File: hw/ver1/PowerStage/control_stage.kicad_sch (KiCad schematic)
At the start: 3 parts, among them J10 SWD Debug, P1 USB_C_Plug_USB2.0, U10 RP2040

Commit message: Sync morning work to laptop
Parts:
- added C18, C21: 4.7uF, Capacitor_SMD:C_0603_1608Metric, symbol Device:C
- added J11: BMS_Serial, Connector_PinHeader_2.54mm:PinHeader_1x03_P2.54mm_Vertical, symbol Connector:Conn_01x03_Pin
- added J8: FanConnector, Connector_Molex:Molex_KK-254_AE-6410-04A_1x04_P2.54mm_Vertical, symbol Connector:Conn_01x04_Pin
- added JP3: I2C_Master, symbol Jumper:SolderJumper_2_Open
- added R92: 10k, Resistor_SMD:R_0603_1608Metric, symbol Device:R_US
- added SW2: I2C_Addr, Button_Switch_SMD:SW_DIP_SPSTx03_Slide_6.7x9.18mm_W6.73mm_P2.54mm_LowProfile_JPin, symbol Switch:SW_DIP_x03
- added U4: LM1117MP-3.3, Package_TO_SOT_SMD:SOT-223-3_TabPin2, symbol Regulator_Linear:LM1117MP-3.3
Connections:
- new net +12P: J8.2 (Pin_2)
- new net +3.3VP: C21.1, R92.2, U4.2 (VO)
- new net +5P: C18.1, U4.3 (VI)
- new net FAN_CTRL: J8.4 (Pin_4)
- new net FAN_SENSE: J8.3 (Pin_3), R92.1
- new net GND: C18.2, C21.2, J8.1 (Pin_1), U4.1 (GND)

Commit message: Sync this morning's effort
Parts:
- added C71, C79: 15pF, Capacitor_SMD:C_0603_1608Metric, symbol Device:C
- added C80, C81, C89: 4.7uF, Capacitor_SMD:C_0603_1608Metric, symbol Device:C
- added C82, C83, C84, C85, C86, C87, C88, C90, C91, C92, C93: 100nF, Capacitor_SMD:C_0603_1608Metric, symbol Device:C
- added D4: B5819W, Diode_SMD:D_SOD-123, symbol Device:D_Schottky
- added R107: 1k, Resistor_SMD:R_0603_1608Metric, symbol Device:R_US
- added R108, R109: 5.1k, Resistor_SMD:R_0603_1608Metric, symbol Device:R_US
- added R24, R26: 22, Resistor_SMD:R_0603_1608Metric, symbol Device:R_US
- added R28, R30: 10k, Resistor_SMD:R_0603_1608Metric, symbol Device:R_US
- added SW3: Boot, symbol Switch:SW_Push
- added SW4: Reset, symbol Switch:SW_Push
- added U20: W25Q32JVZP, Package_SON:WSON-8-1EP_6x5mm_P1.27mm_EP3.4x4.3mm, symbol Memory_Flash:W25Q32JVZP
- added U21: LM1117MP-5.0, Package_TO_SOT_SMD:SOT-223-3_TabPin2, symbol Regulator_Linear:LM1117MP-5.0
- added Y1: 12MHz, Crystal:Crystal_SMD_3225-4Pin_3.2x2.5mm_HandSoldering, symbol Device:Crystal_GND24
- P1: symbol Connector:USB_C_Plug_USB2.0 -> Connector:USB_C_Receptacle_USB2.0_16P
- U4: LCSC C23984 -> C6186
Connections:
- net +3.3VP is gone; now on net +3.3V: C21.1, R92.2, U4.2 (VO)
- net GND: now also J10.3 (Pin_3), P1.A1 (GND), P1.A12 (GND), P1.B1 (GND), P1.B12 (GND), P1.S1 (SHIELD), U10.19 (TESTEN), U10.57 (GND), C71.1, C79.1, C80.2, C81.2, C82.2, C83.2, C84.2, C85.2, C86.2, C87.2, C88.2, C89.2, C90.2, C91.2, C92.2, C93.2, R108.1, R109.1, SW3.1, SW4.1, U20.4 (GND), U20.9 (EP), U21.1 (GND), Y1.2, Y1.4
- net +3.3V: now reaches U10.1 (IOVDD), U10.10 (IOVDD), U10.22 (IOVDD), U10.33 (IOVDD), U10.42 (IOVDD), U10.49 (IOVDD)
- net +3.3V: now also U10.43 (ADC_AVDD), U10.44 (VREG_IN), U10.48 (USB_VDD), C81.1, C82.1, C83.1, C84.1, C85.1, C86.1, C87.1, C88.1, C92.1, R28.2, U20.8 (VCC)
- net at U10.20 (XIN): now also C79.2, Y1.1
- net at U10.21 (XOUT): now also R107.2
- net at U10.23 (DVDD), U10.50 (DVDD): now also U10.45 (VREG_VOUT), C89.1, C90.1, C91.1
- net at U10.24 (SWCLK): now also J10.1 (Pin_1)
- net at U10.25 (SWD): now also J10.2 (Pin_2)
- net RUN: now reaches U10.26 (RUN)
- net RUN: now also C93.1, R28.1, SW4.2
- net at U10.46 (USB_DM): now also R26.1
- net at U10.47 (USB_DP): now also R24.1
- net at U10.51 (QSPI_SD3): now also U20.7 (IO3)
- net at U10.52 (QSPI_SCLK): now also U20.6 (CLK)
- net at U10.53 (QSPI_SD0): now also U20.5 (DI(IO0))
- net at U10.54 (QSPI_SD2): now also U20.3 (IO2)
- net at U10.55 (QSPI_SD1): now also U20.2 (DO(IO1))
- net QSPI_SS: now reaches U10.56 (QSPI_SS)
- net QSPI_SS: now also R30.2, U20.1 (~{CS})
- net at P1.A4 (VBUS), P1.A9 (VBUS), P1.B4 (VBUS)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: now also D4.2 (A)
- net at P1.A5 (CC1): now also R108.2
- net USB_D+: now reaches P1.A6 (D+)
- net USB_D+: now also P1.B6 (D+), R24.2
- net USB_D-: now reaches P1.A7 (D-)
- net USB_D-: now also P1.B7 (D-), R26.2
- net at P1.B5 (CC2): now also R109.2
- net +12P renamed +12V
- net +12V: now also C80.1, U21.3 (VI)
- net +5P renamed +5V
- net +5V: now also D4.1 (K), U21.2 (VO)
- new net: R30.1, SW3.2
- new net: C71.2, R107.1, Y1.3
- no-connect marks 0 -> 2
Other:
- note added: "Add some nice leds"
- moved on the sheet: C18, C21, J10, J11, U10, U4

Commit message: Sync tonight's effort
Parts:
- removed JP3: I2C_Master, symbol Jumper:SolderJumper_2_Open
- added C94: 4.7uF, Capacitor_SMD:C_0603_1608Metric, symbol Device:C
- added D5, D6: Yellow LED, LED_SMD:LED_0805_2012Metric, symbol Device:LED
- added R110, R111, R112, R113, R114, R115: 0, Resistor_SMD:R_0603_1608Metric, symbol Device:R_US
- added R116, R126, R127, R130: 100k, Resistor_SMD:R_0603_1608Metric, symbol Device:R_US
- added R117, R118, R119, R121, R122, R123, R128: 1k, Resistor_SMD:R_0603_1608Metric, symbol Device:R_US
- added R120, R124, R125, R129: 2k, Resistor_SMD:R_0603_1608Metric, symbol Device:R_US
- added R131, R132: 510, Resistor_SMD:R_0603_1608Metric, symbol Device:R_US
- D4: Digikey (none) -> N/A
- J10, J11: Digikey (none) -> N/A; LCSC (none) -> N/A
- J8, P1, U20, Y1: LCSC (none) -> N/A
- SW3, SW4: footprint (none) -> Button_Switch_SMD:SW_SPST_EVQP2; Digikey (none) -> P11081SCT-ND; LCSC (none) -> N/A
- U10: Digikey (none) -> 2648-SC0914(13)CT-ND; LCSC (none) -> C2040
- U21: Digikey (none) -> N/A; LCSC (none) -> C6187
- U4: Digikey 488-LM1117MPX-33NOPBCT-ND -> N/A
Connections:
- net +3.3V: now also R126.2, R127.2, R130.2
- net +5V: now also R131.1, R132.1
- net FAN_CTRL: now also U10.8 (GPIO6), R121.2; no longer J8.4 (Pin_4)
- net FAN_SENSE: now also U10.4 (GPIO2)
- net GND: now also J11.3 (Pin_3), SW2.4, SW2.5, SW2.6, C94.2, R120.1, R124.1, R125.1, R129.1
- net at U10.11 (GPIO8): now also R115.2
- net at U10.12 (GPIO9): now also R114.2
- net SPI1_SCK: now reaches U10.13 (GPIO10)
- net SPI1_SCK: now also R113.2
- net SPI1_TX: now reaches U10.14 (GPIO11)
- net SPI1_TX: now also R110.2
- net SPI1_RX: now reaches U10.15 (GPIO12)
- net SPI1_RX: now also R112.2
- net SPI1_CSn: now reaches U10.16 (GPIO13)
- net SPI1_CSn: now also R111.2
- net CTL_OUT_SYNC: now reaches U10.17 (GPIO14)
- net CTL_OUT_RUN: now reaches U10.18 (GPIO15)
- net at U10.2 (GPIO0): now also R116.2
- net CTL_OUT_CCM: now reaches U10.27 (GPIO16)
- net CTL_OUT_DCM: now reaches U10.28 (GPIO17)
- net LED_STATUS_0: now reaches U10.29 (GPIO18)
- net LED_STATUS_0: now also D6.1 (K)
- net LED_STATUS_1: now reaches U10.30 (GPIO19)
- net LED_STATUS_1: now also D5.1 (K)
- net I2C_ADDR_0: now reaches U10.31 (GPIO20)
- net I2C_ADDR_0: now also SW2.1, R126.1
- net I2C_ADDR_1: now reaches U10.32 (GPIO21)
- net I2C_ADDR_1: now also SW2.2, R127.1
- net I2C_ADDR_2: now reaches U10.34 (GPIO22)
- net I2C_ADDR_2: now also SW2.3, R130.1
- net CTL_OUT_ADC_SEL_0: now reaches U10.35 (GPIO23)
- net CTL_OUT_ADC_SEL_1: now reaches U10.36 (GPIO24)
- net CTL_OUT_ADC_SEL_2: now reaches U10.37 (GPIO25)
- net CTL_IN_ADC: now reaches U10.38 (GPIO26_ADC0)
- net UART1_TX: now reaches U10.6 (GPIO4)
- net UART1_TX: now also R118.2
- net UART1_RX: now reaches U10.7 (GPIO5)
- net UART1_RX: now also R117.2
- net at J11.1 (Pin_1): now also R118.1
- net at J11.2 (Pin_2): now also R117.1
- new net: D6.2 (A), R131.2
- new net: J8.4 (Pin_4), R121.1
- new net: D5.2 (A), R132.2
- new net: R112.1, R119.1, R120.2
- new net CTL_IN_FAULT: R122.2
- new net CTL_IN_PGOOD: R123.2
- new net CTL_IN_SDI: R119.2
- new net CTL_IN_SLAVE: R128.2
- new net CTL_IO_SDA: R115.1
- new net CTL_OUT_CSB: R111.1
- new net CTL_OUT_SCK: R113.1
- new net CTL_OUT_SCL: R114.1
- new net CTL_OUT_SDO: R110.1
- new net CTL_OUT_SETCUR: C94.1, R116.1
- new net SIG_FAULT: R122.1, R125.2
- new net SIG_PGOOD: R123.1, R124.2
- new net SIG_SLAVE: R128.1, R129.2
- no-connect marks 2 -> 8
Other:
- note added: "Cutoff Freq 0.33Hz"
- note added: "I2C0"
- note added: "PWM 0A"
- note added: "PWM 1A"
- note added: "PWM 3A"
- note added: "PWM 7A"
- note removed: "Add some nice leds"
- note removed: "Make sure to add zero ohm resistors on all control lines"
- moved on the sheet: J11, J8, R92, SW2

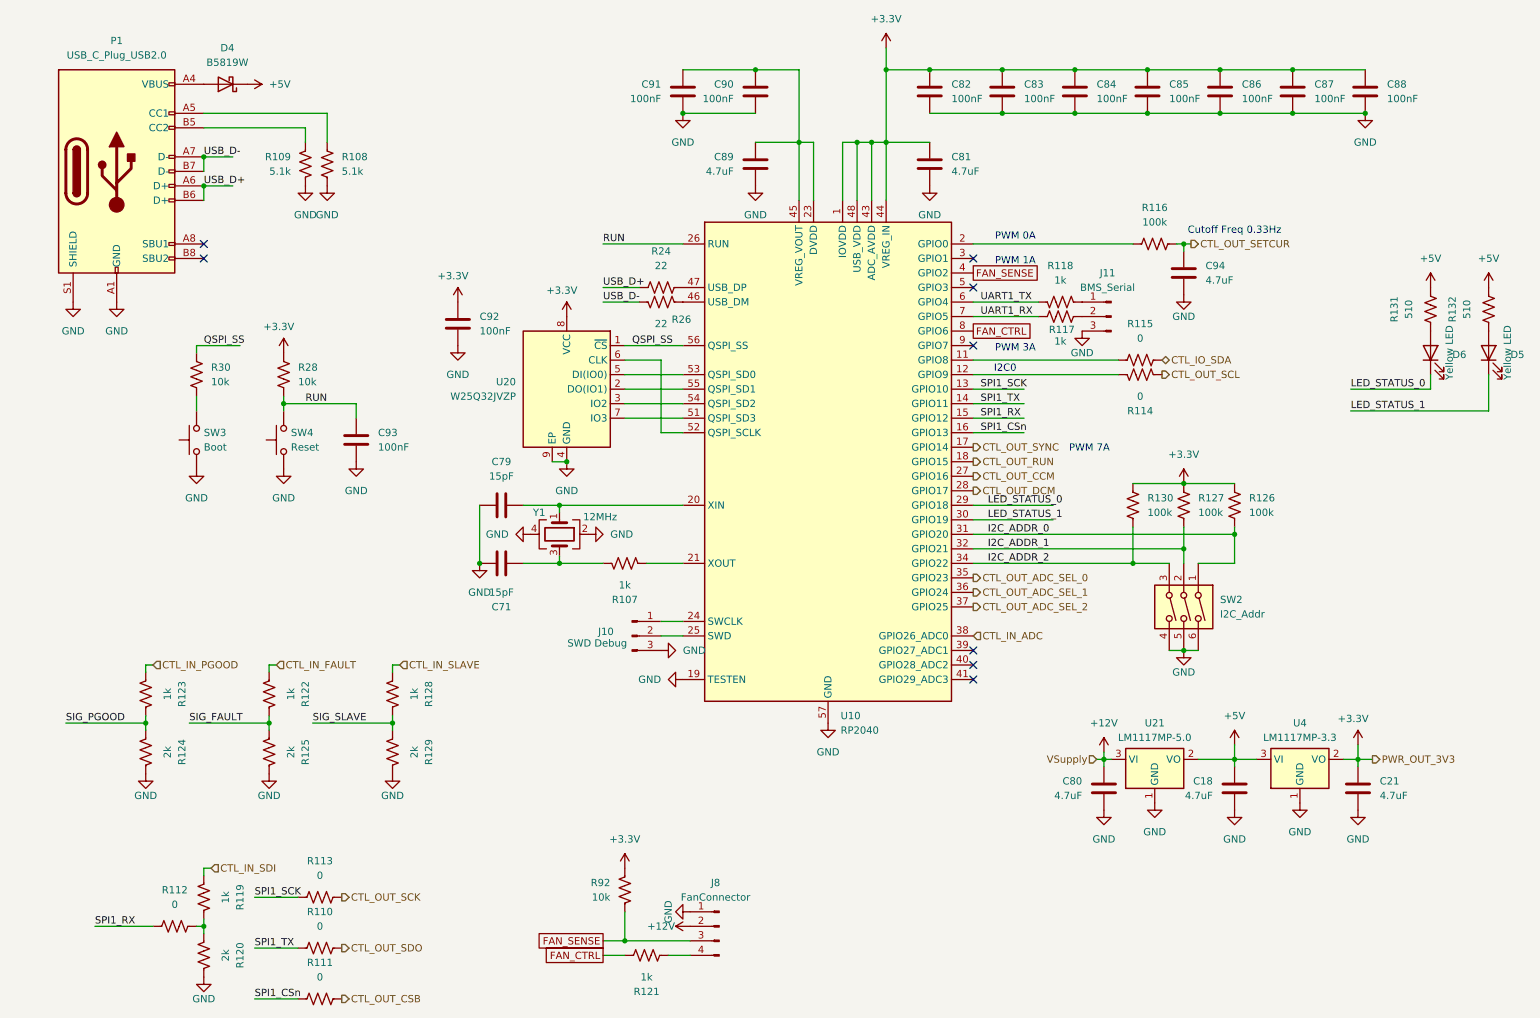
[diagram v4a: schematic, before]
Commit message: Start optimizing some of the layout to make room for control circuitry
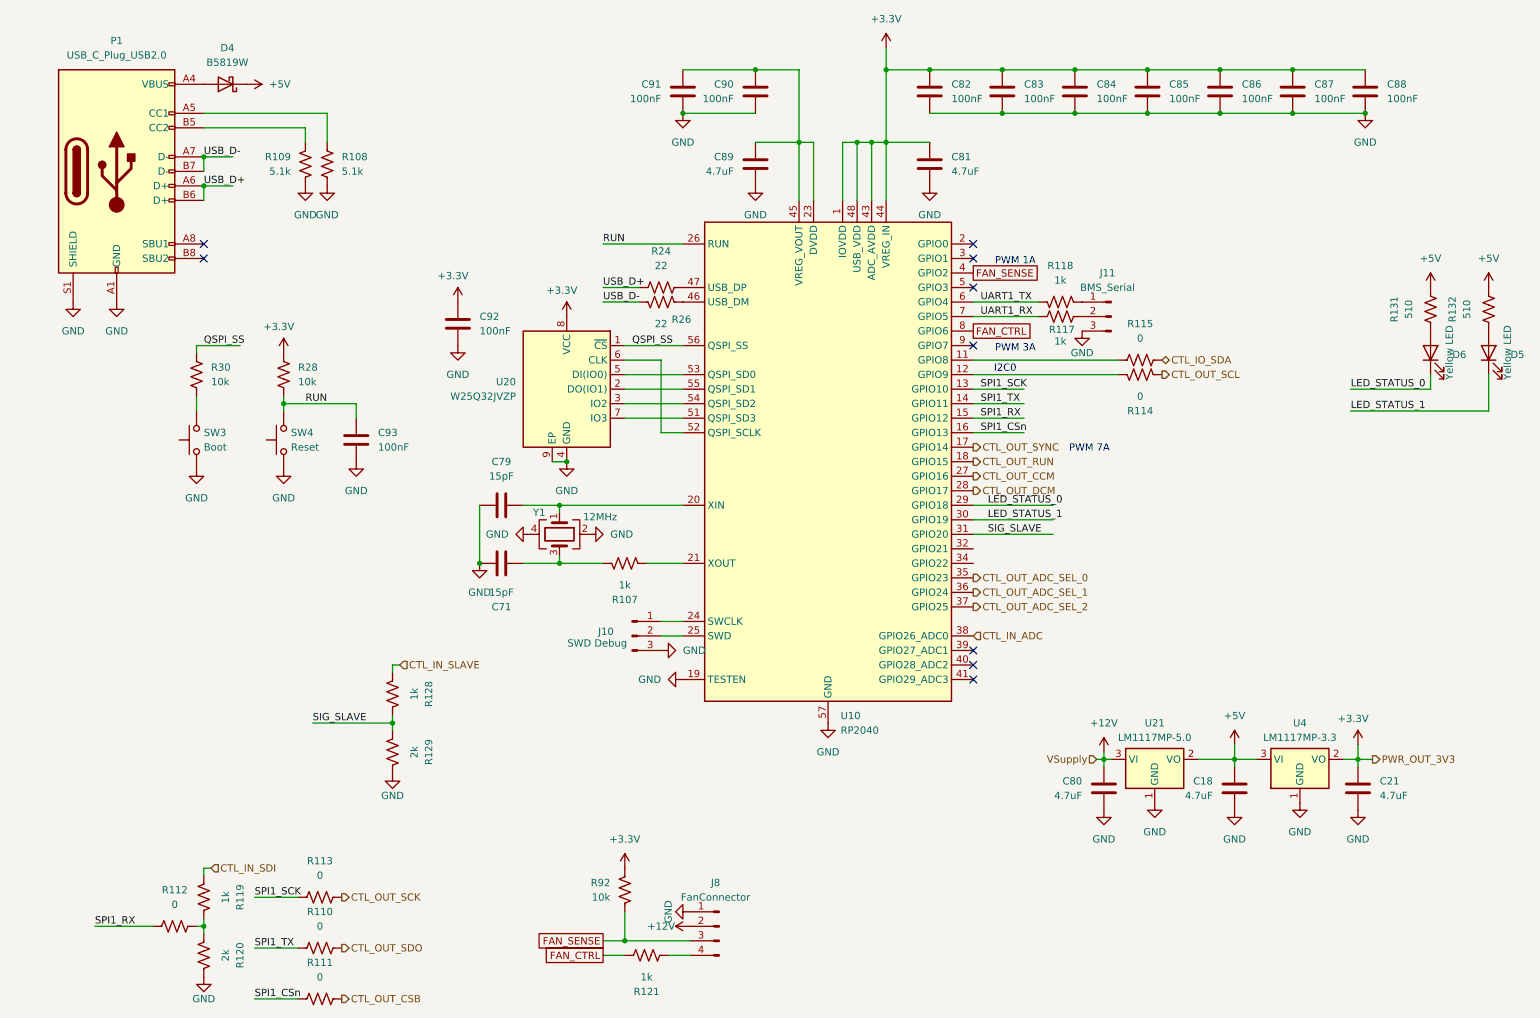
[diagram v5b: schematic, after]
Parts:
- removed C94: 4.7uF, Capacitor_SMD:C_0603_1608Metric, symbol Device:C
- removed R116, R126, R127, R130: 100k, Resistor_SMD:R_0603_1608Metric, symbol Device:R_US
- removed R122, R123: 1k, Resistor_SMD:R_0603_1608Metric, symbol Device:R_US
- removed R124, R125: 2k, Resistor_SMD:R_0603_1608Metric, symbol Device:R_US
- removed SW2: I2C_Addr, Button_Switch_SMD:SW_DIP_SPSTx03_Slide_6.7x9.18mm_W6.73mm_P2.54mm_LowProfile_JPin, symbol Switch:SW_DIP_x03
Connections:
- net I2C_ADDR_0 is gone; now on net SIG_SLAVE: U10.31 (GPIO20)
- net I2C_ADDR_1: no longer names the net of U10.32 (GPIO21)
- net I2C_ADDR_2: no longer names the net of U10.34 (GPIO22)
- no-connect marks 8 -> 9
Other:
- note removed: "Cutoff Freq 0.33Hz"
- note removed: "PWM 0A"

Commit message: Sync work
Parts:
- removed R114, R115: 0, Resistor_SMD:R_0603_1608Metric, symbol Device:R_US
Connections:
- net CTL_IO_SDA: now also U10.2 (GPIO0)
- net CTL_OUT_ADC_SEL_0: now also U10.7 (GPIO5); no longer U10.35 (GPIO23)
- net CTL_OUT_ADC_SEL_1: now also U10.8 (GPIO6); no longer U10.36 (GPIO24)
- net CTL_OUT_ADC_SEL_2: now also U10.9 (GPIO7); no longer U10.37 (GPIO25)
- net CTL_OUT_CCM: now also U10.5 (GPIO3); no longer U10.27 (GPIO16)
- net CTL_OUT_DCM: now also U10.4 (GPIO2); no longer U10.28 (GPIO17)
- net CTL_OUT_SCL: now also U10.3 (GPIO1)
- net CTL_OUT_SYNC: now also U10.6 (GPIO4); no longer U10.17 (GPIO14)
- net FAN_CTRL: no longer U10.8 (GPIO6)
- net FAN_SENSE: no longer U10.4 (GPIO2)
- net UART1_RX: now also U10.37 (GPIO25); no longer U10.7 (GPIO5)
- net UART1_TX: now also U10.36 (GPIO24); no longer U10.6 (GPIO4)
- net SWCLK: now reaches J10.1 (Pin_1), U10.24 (SWCLK)
- net SWDATA: now reaches J10.2 (Pin_2), U10.25 (SWD)
- no-connect marks 9 -> 7
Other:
- note added: "PWM2A"
- note removed: "PWM 3A"
- note removed: "PWM 7A"
- moved on the sheet: J10, J11, R117, R118

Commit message: Sync yesterday's effort
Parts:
- removed R111, R113: 0, Resistor_SMD:R_0603_1608Metric, symbol Device:R_US
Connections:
- net SPI1_CSn is gone; now on net CTL_OUT_CSB: U10.16 (GPIO13)
- net SPI1_SCK is gone; now on net CTL_OUT_SCK: U10.13 (GPIO10)
- net CTL_OUT_RUN: now also U10.37 (GPIO25); no longer U10.18 (GPIO15)
- net SIG_SLAVE: now also U10.36 (GPIO24); no longer U10.31 (GPIO20)
- net UART0_TX: now reaches U10.27 (GPIO16)
- net UART0_TX: now also R118.2
- net UART0_RX: now reaches U10.28 (GPIO17)
- net UART0_RX: now also R117.2
- removed net UART1_RX: R117.2, U10.37 (GPIO25)
- removed net UART1_TX: R118.2, U10.36 (GPIO24)
- no-connect marks 7 -> 8
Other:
- moved on the sheet: J11, R117, R118
